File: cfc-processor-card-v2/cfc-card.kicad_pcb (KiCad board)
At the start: 4 copper layers, 99.8 x 94.6 mm, 273 parts, among them J1 ORESAT-DEBUG-CONNECTOR-ALL, J100 DM3BT-DSF-PEJS, J2 J-SAMTEC-TFM-110-X1-XXX-D-RA, J3 CONN_03LONGPADS, J4 TFM-120-01-L-D-RA, Q1 MMBT2907, Q2 PMV45EN, Q3 DMP2240UDM, Q4 PMV45EN, Q5 MOSFET-PCH-SOT23-6, Q6 MOSFET-PCH-SOT23-6, U1 RCLAMP0504FB, U10 TLVH431, U11 TCAN330, U12 MIC842LYC5, U13 MIC842LYC5, U14 MAX4211FETE, U15 TPS62112, U16 MAX7310ATE, U17 25AAXX, U2 DS90CR218AMTD/NOPBMTD48_TEX-L, U3 THGBMJG7C2LBAU8, U4 SN74LVC1G07DCK, U5 TS5A21366, U7 OSD3358-512M-BSM, Y1 24MHz, Y2 ABS07-32.768KHZ-T

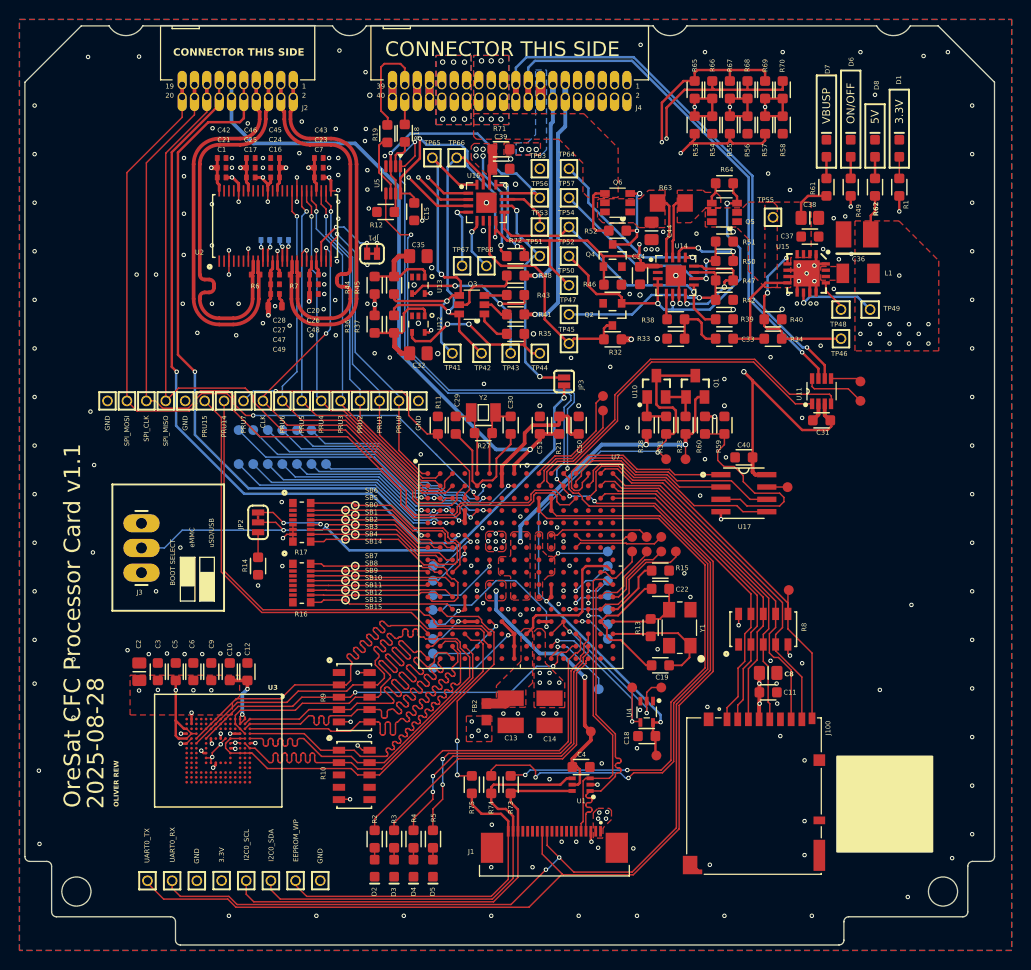
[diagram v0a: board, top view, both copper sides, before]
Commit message: more trace polishing.
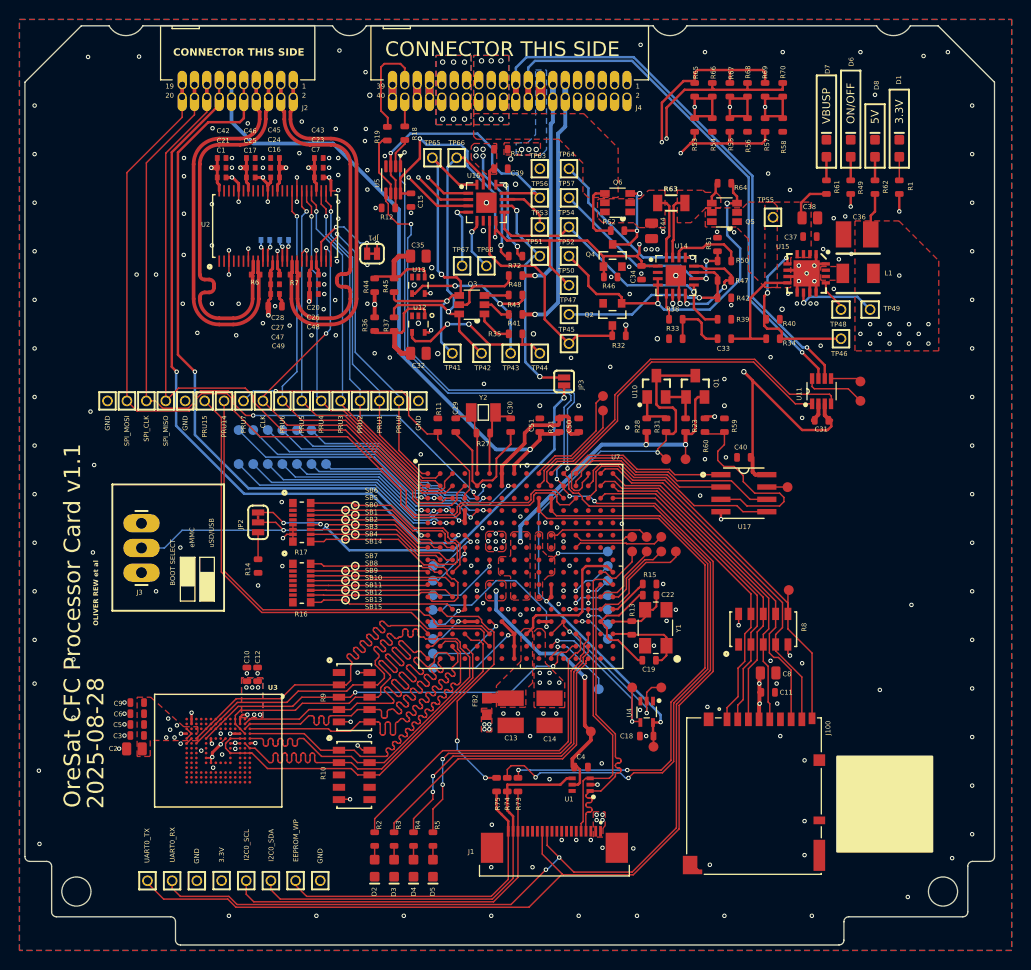
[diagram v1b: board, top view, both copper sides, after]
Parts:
- C1, C16, C17, C20, C21, C23, C24, C25, C26, C27, C28, C42, C43, C45, C46, C47, C48, C7, R29, R30, R6, R7: footprint cfc-card:.0402-C-NOSILK -> oresat-passives:0402-C-NOSILK
- C10, C11, C12, C15, C18, C19, C22, C29, C3, C30, C31, C33, C34, C37, C39, C4, C40, C5, C50, C51, C6, C9, R1, R11, R12, R13, R14, R15, R18, R19, R2, R21, R23, R27, R28, R3, R31, R32, R33, R34, R35, R36, R37, R38, R39, R4, R40, R41, R42, R43, R44, R45, R46, R47, R48, R49, R5, R50, R51, R52, R53, R54, R55, R56, R57, R58, R59, R60, R61, R62, R64, R65, R66, R67, R68, R69, R70, R71, R72, R73, R74, R75: footprint cfc-card:.0603-A -> oresat-passives:0603-C-NOSILK
- C2, C38, C44, C8: footprint cfc-card:.0805-B -> oresat-passives:0805-C-NOSILK
- C32, C35: footprint cfc-card:.0805-B-NOSILK -> oresat-passives:0805-C-NOSILK
- C49: footprint cfc-card:.0603-C-NOSILK -> oresat-passives:0603-C-NOSILK
- R63: footprint cfc-card:R1206_334 -> oresat-passives:1206-C
- moved C9 8.26 mm to (110.2, 127.4), turned to 180 degrees
- moved C2 7.96 mm to (109.9, 132.1), turned to 180 degrees
- moved C6 7.21 mm to (110.2, 128.5), turned to 180 degrees
- moved C3 6.90 mm to (110.2, 130.7), turned to 180 degrees
- moved C5 6.73 mm to (110.2, 129.6), turned to 180 degrees
- moved R75 2.55 mm to (147.2, 135.8)
- moved Y1 2.47 mm to (163.5, 119.7)
- moved R13 1.95 mm to (161.1, 119.7)
- moved C10 1.78 mm to (121.5, 124.5)
- moved R15 1.77 mm to (162.9, 115.2)
- moved R74 1.65 mm to (148.2, 135.8)
- moved C22 1.29 mm to (162.9, 116.3)
- moved C19 1.27 mm to (162.8, 123.0)
- moved C15 1.23 mm to (138.3, 75.6)
- moved C12 1.08 mm to (122.5, 124.5)
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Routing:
- net 3.3V: track 87.0 -> 78.1 mm
- net I2C0_SCL: track 46.1 -> 39.6 mm
- net Net-(U3-VDDI): track 7.90 -> 1.56 mm, vias 2 -> 6
- net GND: track 57.8 -> 53.8 mm, vias 260 -> 266
- net /OSD3358: SIP B (USB, XTAL, ADC)/OSC0_IN: track 12.5 -> 8.82 mm
- net VPD: track 77.8 -> 74.5 mm
- net UART0_TX: track 167.4 -> 164.1 mm
- net I2C0_SDA: track 46.7 -> 44.0 mm
- net /OSD3358: SIP B (USB, XTAL, ADC)/OSC0_GND: track 14.3 -> 12.0 mm
- net Net-(U7A-RTC_KALDO_ENN): track 6.31 -> 4.15 mm
- net EEPROM_WP: track 35.1 -> 33.1 mm
- net /Power (OPD)/ON/~{OFF}: track 79.5 -> 77.6 mm
- net Net-(U7A-I2C0_SDA): track 63.1 -> 61.2 mm
- net /OSD3358: SIP B (USB, XTAL, ADC)/OSC0_OUT: track 8.44 -> 6.72 mm
- net THERM+: track 65.6 -> 64.3 mm
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- added copper zone on B.Cu, net Net-(U3-VDDI)
- added copper zone on F.Cu, net Net-(U3-VDDI)
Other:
- board text added: "OLIVER REW et al"
- board text removed: "OLIVER REW"

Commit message: More layout polishing Removed unused SPI EEPROM.
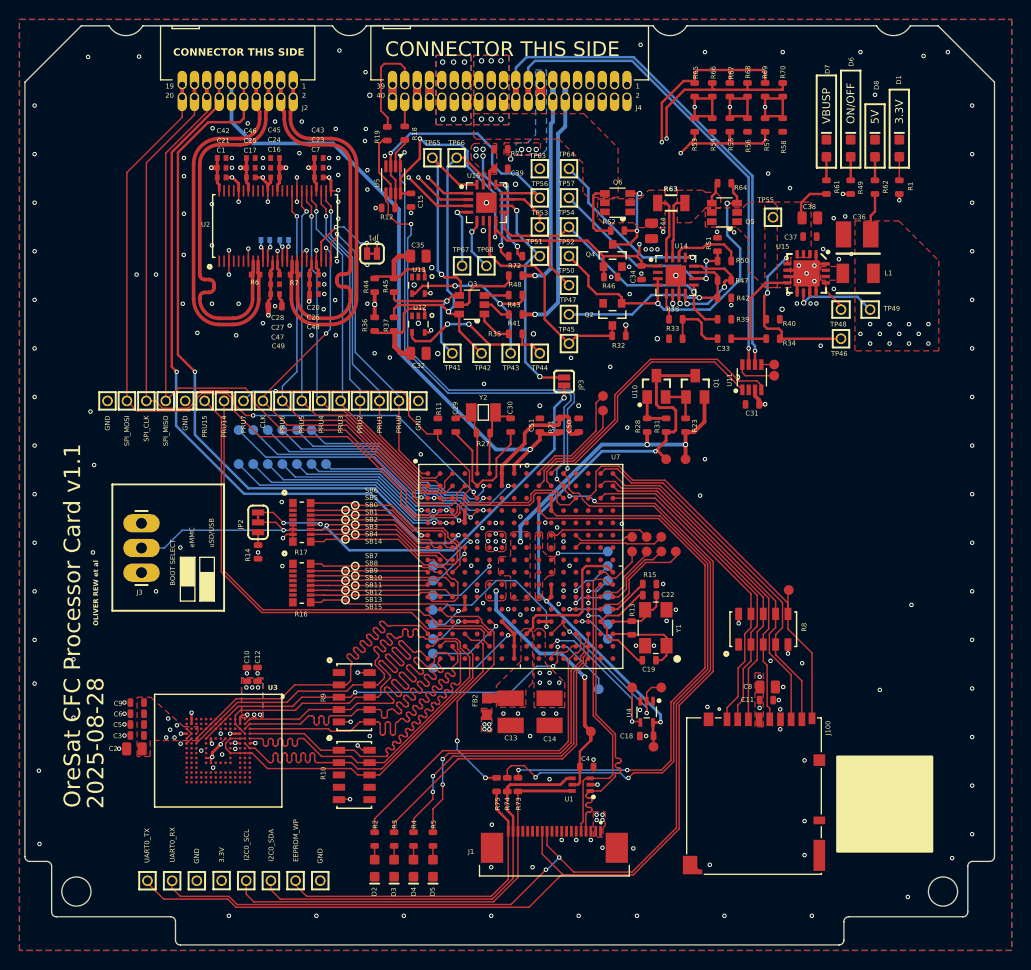
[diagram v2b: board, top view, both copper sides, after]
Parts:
- removed C40, R59, R60: DNP, oresat-passives:0603-C-NOSILK
- removed TP69: TEST-POINT3X4, cfc-card:PAD.03X.04
- removed U17: 25AAXX, cfc-card:SOIC8
- C4: value 0.1uF -> 100n
- moved TP40 9.25 mm to (175.7, 93.7)
- moved TP35 9.05 mm to (175.7, 92.6)
- moved U11 7.32 mm to (173.4, 93.9)
- moved C31 7.31 mm to (173.5, 96.7)
- moved R14 1.45 mm to (122.6, 111.8)
- moved C8 1.45 mm to (175.1, 125.8)
- moved C11 0.82 mm to (174.9, 127.1)
- moved C4 0.57 mm to (156.4, 134.0)
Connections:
- U7 pad A13: Net-(U17-SCK) -> unconnected-(U7C-SPI0_SCLK-PadA13)
- U7 pad A14: Net-(U17-~{CS}) -> unconnected-(U7C-SPI0_CS0-PadA14)
- U7 pad B13: Net-(U17-MISO) -> unconnected-(U7C-SPI0_D0-PadB13)
- U7 pad B14: Net-(U17-MOSI) -> unconnected-(U7C-SPI0_D1-PadB14)
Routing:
- net 3.3V: track 78.1 -> 46.3 mm, vias 32 -> 31
- net Net-(U17-SCK): track 22.1 -> 0.00 mm
- net Net-(U17-MOSI): track 22.0 -> 0.00 mm
- net Net-(U17-~{CS}): track 21.6 -> 0.00 mm
- net Net-(U17-~{WP}): track 21.2 -> 0.00 mm
- net Net-(U17-MISO): track 17.6 -> 0.00 mm
- net Net-(U11-RXD): track 39.6 -> 31.6 mm
- net Net-(U11-TXD): track 34.9 -> 27.1 mm
- net I2C0_SCL: track 39.6 -> 45.2 mm
- net CAN2_L: track 57.1 -> 52.4 mm
- net CAN2_H: track 54.7 -> 50.3 mm
- net GND: track 53.8 -> 51.1 mm, vias 266 -> 260
- net Net-(TP69-1): track 2.14 -> 0.00 mm
- net Net-(TP40-1): track 6.41 -> 4.30 mm
- net Net-(TP35-1): track 3.15 -> 1.33 mm
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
